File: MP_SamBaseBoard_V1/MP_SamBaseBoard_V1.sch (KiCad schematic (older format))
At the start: 129 parts, among them J1 MA_CONN, J10 P1_CONN, J11 I2C_CONN, J12 I2C_CONN, J13 SAM_SWD, J14 WS2812_EXT, J15 PWR_JACK, J16 USB_B_Micro, J17 BATT_CONN, J2 MB_CONN, J3 Adafruit_Feather_CONN, J4 LOAD_CONN, J5 SPEAKER, J7 SERVO_CONN, J8 P3_CONN, J9 P2_CONN, Q1 DMP3098L, Q2 ALS-PT19-315C/L177/TR8, SW1 RESET, SW2 3v3_PWR_SW, SW3 SW1, SW4 SW2, U1 ESP32-WROOM-32, U10 KXTJ3-1057, U13 SST25VF016B-50-4C-S2AF, U2 ATSAMD51J19A-A, U3 74LVC1G125, U4 TPS62135, U5 PAM8301, U6 BQ24075, U7 DRV8833RTY, U8 Sensirion_SHT3x, U9 LD39200PU33R, Y1 Crystal

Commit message: update
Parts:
- added Q3: BSS138-7-F, Package_TO_SOT_SMD:SOT-23, symbol Device:Q_NMOS_GSD
- added R12: 10K, Resistor_SMD:R_0603_1608Metric, symbol Device:R_Small
- added U12: IRFHM9331PbF, GiraffeTech-IR:PQFN_3x3mm_IRFHM9331TRPbF, symbol InGarage_FETs:IRFHM9331PbF
- gave numbers to parts that had none: 5
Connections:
- net +5V: now also U12.5 (DRAIN), U12.6 (DRAIN), U12.7 (DRAIN), U12.8 (DRAIN); no longer R8.1
- net GND: now also Q3.2 (S)
- net PG_5V: now also Q3.1 (G)
- net VIN: now also R8.1, R12.2, U12.1 (SOURCE), U12.2 (SOURCE), U12.3 (SOURCE)
- new net: Q3.3 (D), R12.1, U12.4 (GATE)
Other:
- moved on the sheet: BZ1, C10, C12, C13, C15, C16, C18, C29, C30, C31, C34, C35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

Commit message: finalize 1
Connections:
- net +3V3: no longer U10.3 (IO_VDD), U10.7 (VDD)
- no-connect marks 42 -> 44
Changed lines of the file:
@@
 Wire Wire Line
 	3750 9850 4500 9850
-Wire Wire Line
-	3750 9750 3750 9850
-Wire Wire Line
-	3750 9750 4500 9750
 Connection ~ 3750 9850
 NoConn ~ 5500 10200
@@
 $EndComp
 Wire Wire Line
-	3750 9650 3750 9750
-Connection ~ 3750 9750
-Wire Wire Line
-	4200 10000 4500 10000
-Wire Wire Line
-	4200 10100 4200 10000
-Wire Wire Line
 	3750 9850 3750 10200
 $Comp
@@
 	1    0    0    -1
 $EndComp
-Wire Wire Line
-	4200 9650 4200 10000
-Connection ~ 4200 10000
 Text Notes 9000 9350 0    50   ~ 0
 LIGHT SENSOR
@@
 	12150 1800 12150 1850
 Connection ~ 12150 1800
+Wire Wire Line
+	3750 9650 3750 9850
+Wire Wire Line
+	4200 9650 4200 10100
+Wire Wire Line
+	4400 9750 4500 9750
+Wire Wire Line
+	4400 10000 4500 10000
+NoConn ~ 4400 9750
+NoConn ~ 4400 10000
 $EndSCHEMATC

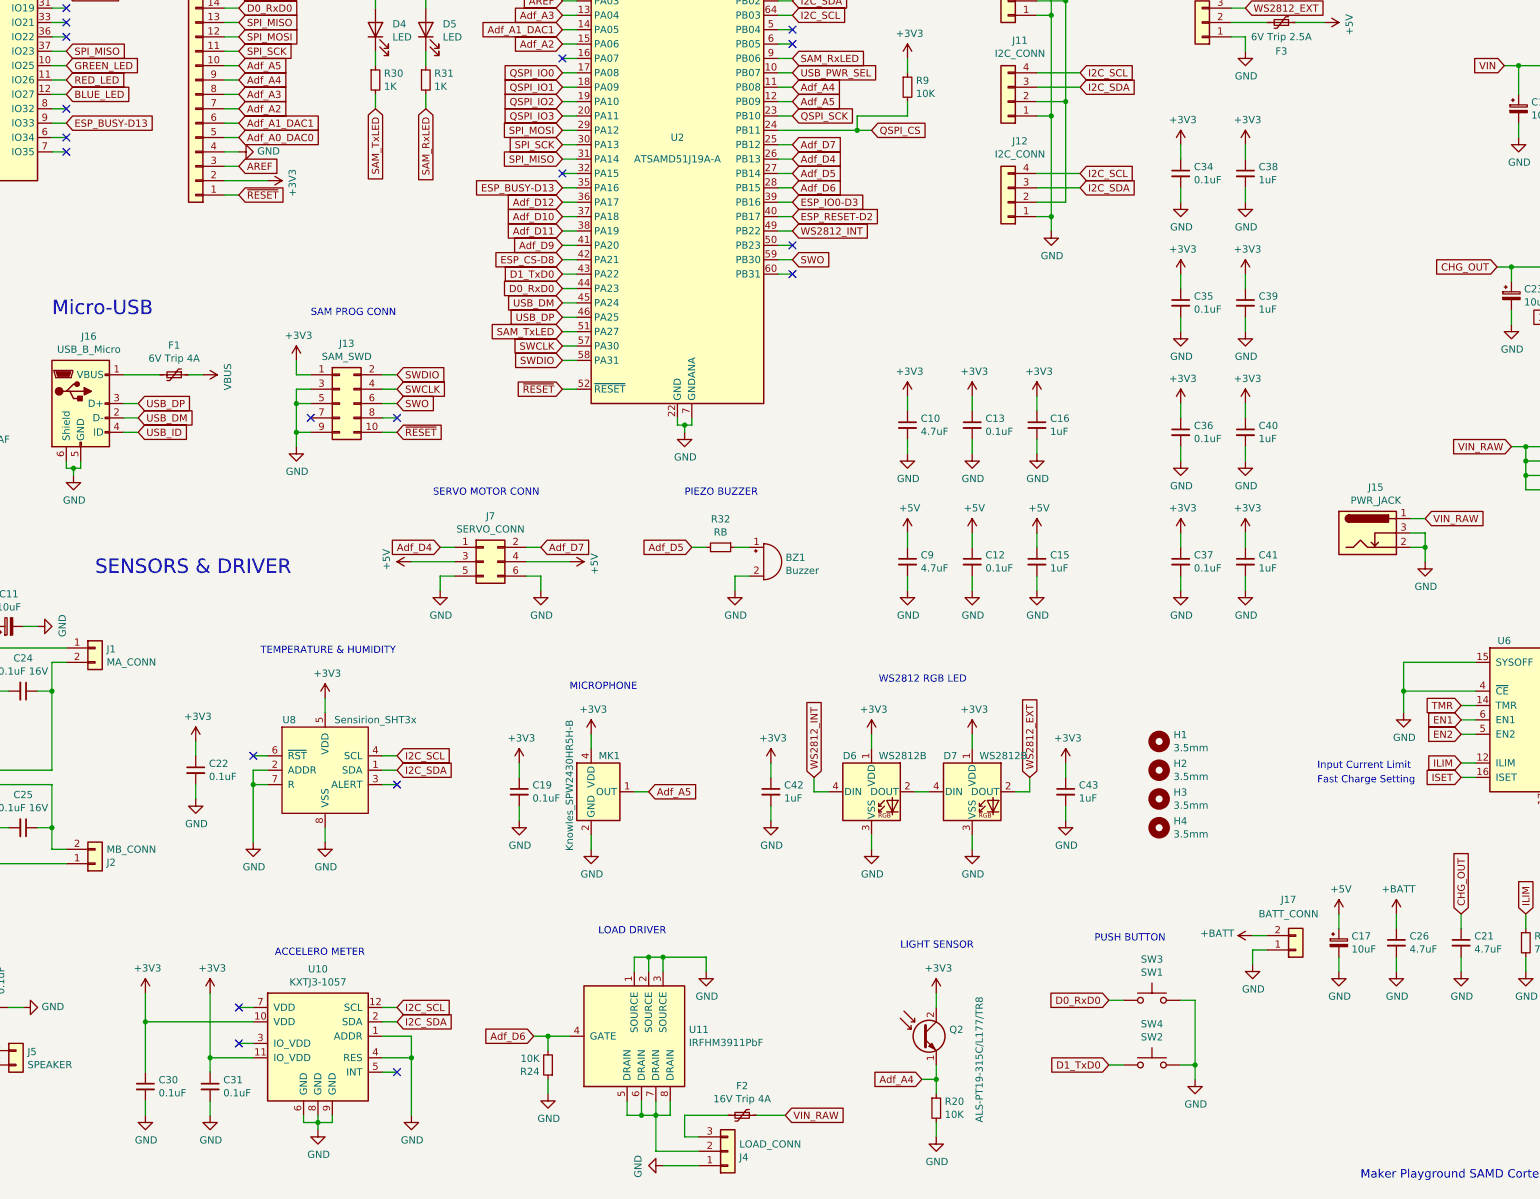
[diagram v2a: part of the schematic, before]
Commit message: Adding OLED display in progress
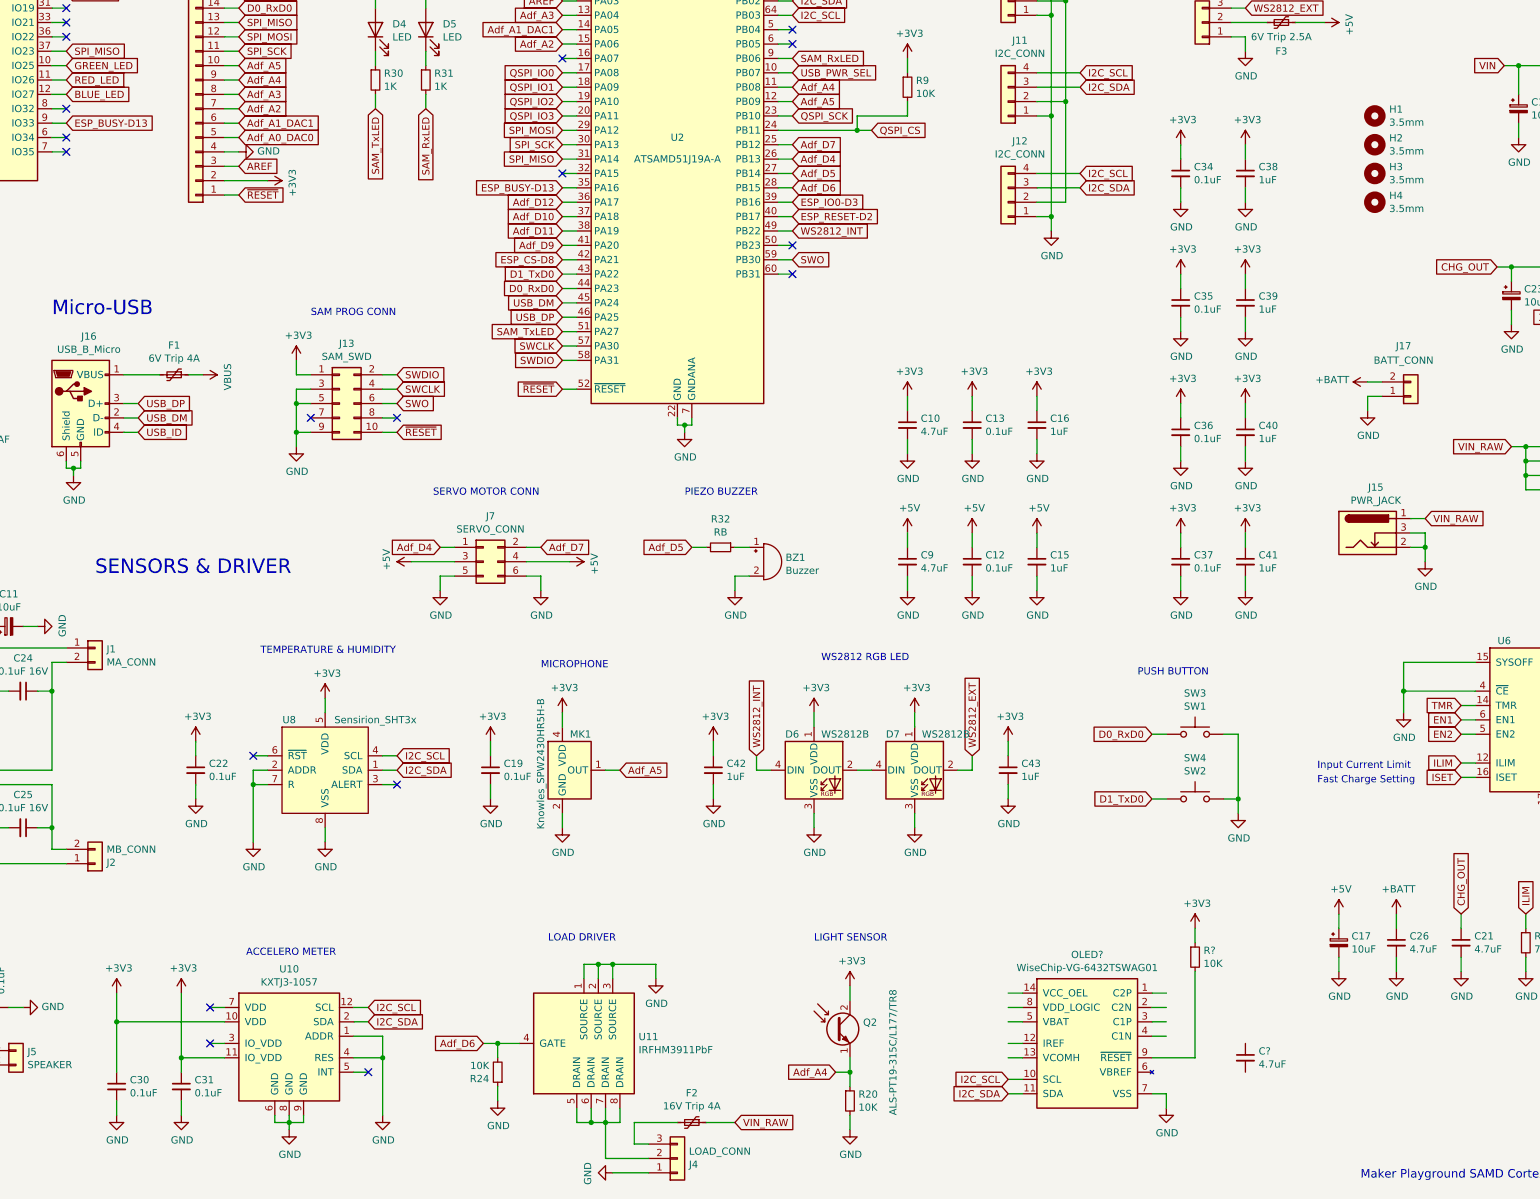
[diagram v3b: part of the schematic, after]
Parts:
- added C?: 4.7uF, Capacitor_SMD:C_0603_1608Metric, symbol Device:C_Small
- added OLED?: WiseChip-VG-6432TSWAG01, GiraffeTech-Connector:WiseChip-VG-6432TSWAG01, symbol InGarage_Display:WiseChip-VG-6432TSWAG01
- added R?: 10K, Resistor_SMD:R_0603_1608Metric, symbol Device:R_Small
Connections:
- net +3V3: now also R?.1
- net GND: now also OLED?.7 (VSS)
- net I2C_SCL: now also OLED?.10 (SCL)
- net I2C_SDA: now also OLED?.11 (SDA)
- new net: OLED?.9 (~RESET), R?.2
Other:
- moved on the sheet: C19, C30, C31, C42, C43, D6, D7, F2, H1, H2, H3, H4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

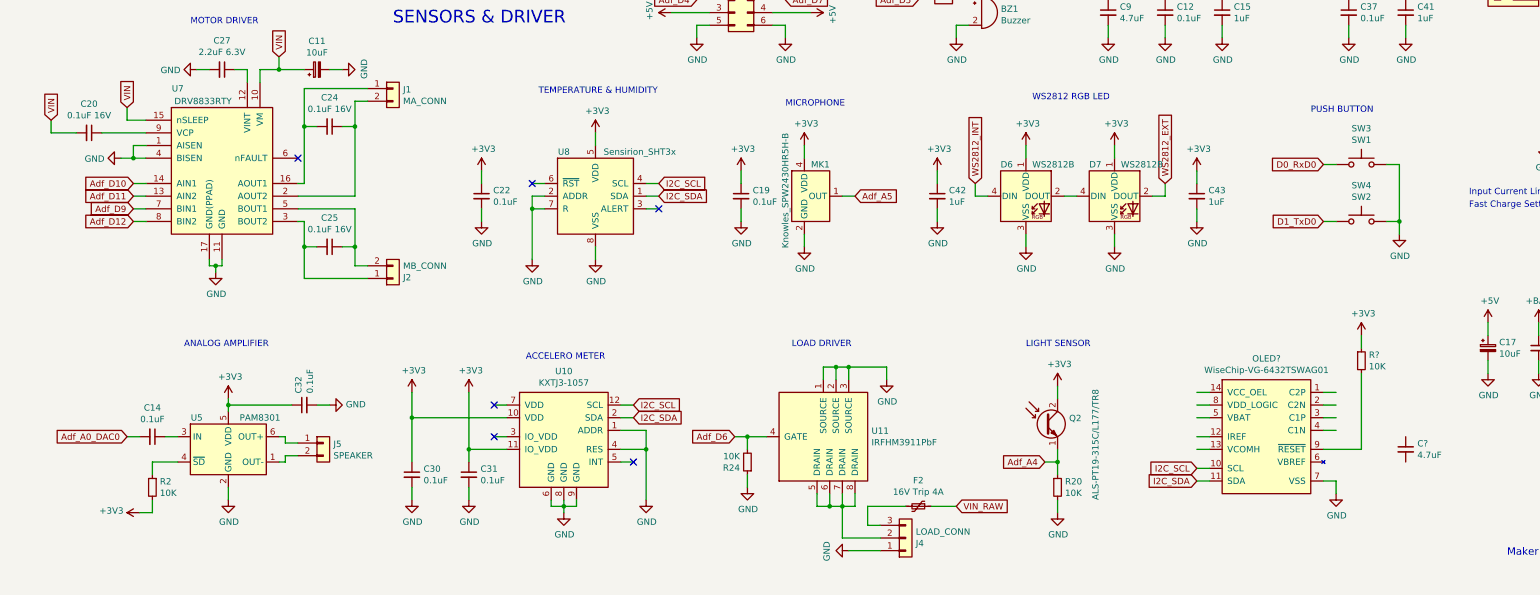
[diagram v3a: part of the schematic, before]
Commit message: Update OLED display, not complete
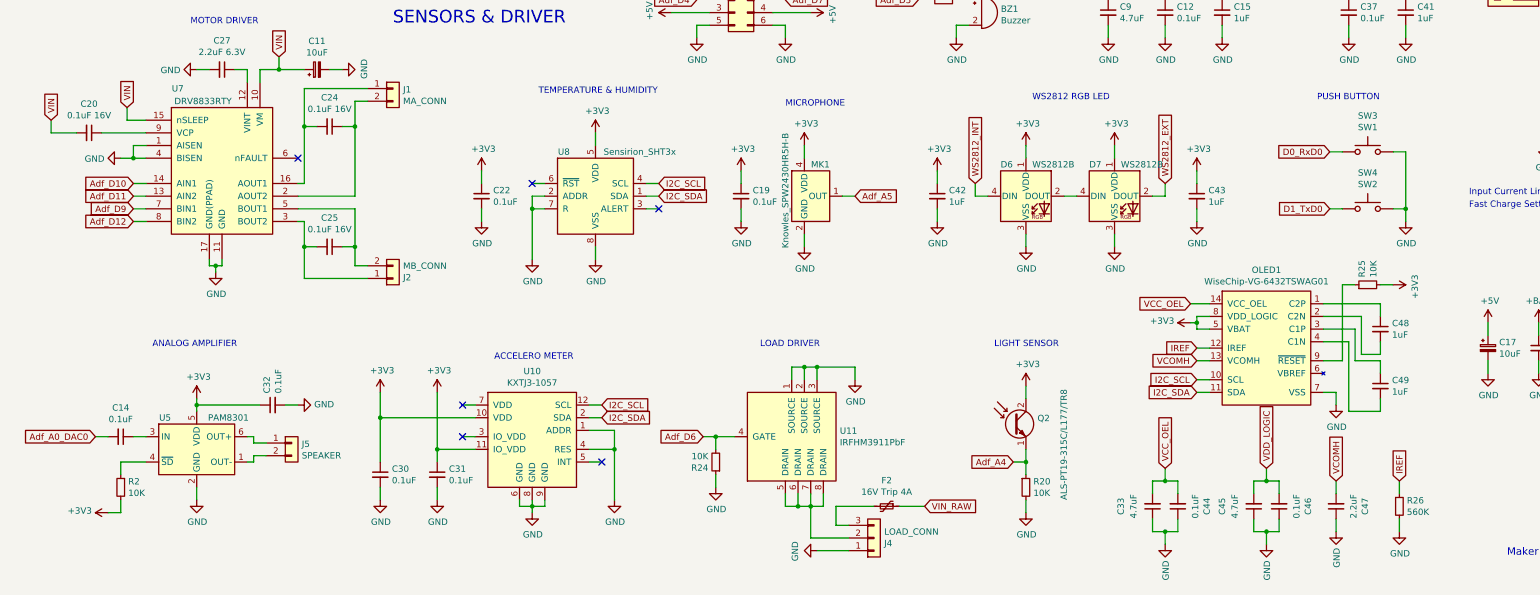
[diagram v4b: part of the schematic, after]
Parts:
- added C33, C45: 4.7uF, Capacitor_SMD:C_0603_1608Metric, symbol Device:C_Small
- added C44, C46: 0.1uF, Capacitor_SMD:C_0603_1608Metric, symbol Device:C_Small
- added C47: 2.2uF, Capacitor_SMD:C_0603_1608Metric, symbol Device:C_Small
- added C49: 1uF, Capacitor_SMD:C_0603_1608Metric, symbol Device:C_Small
- added R26: 560K, Resistor_SMD:R_0603_1608Metric, symbol Device:R_Small
- C48: renamed from C?; value 4.7uF -> 1uF
- gave numbers to parts that had none: 2
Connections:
- net +3V3: now also OLED1.5 (VBAT), OLED1.8 (VDD_LOGIC), R25.2; no longer R25.1
- net GND: now also C33.1, C44.1, C45.1, C46.1, C47.1, R26.2
- net at OLED1.1 (C2P): now also C48.1
- net IREF: now reaches OLED1.12 (IREF)
- net IREF: now also R26.1
- net VCOMH: now reaches OLED1.13 (VCOMH)
- net VCOMH: now also C47.2
- net VCC_OEL: now reaches OLED1.14 (VCC_OEL)
- net VCC_OEL: now also C33.2, C44.2
- net at OLED1.2 (C2N): now also C48.2
- net at OLED1.3 (C1P): now also C49.1
- net at OLED1.4 (C1N): now also C49.2
- net at OLED1.9 (~RESET): now also R25.1; no longer R25.2
- new net VDD_LOGIC: C45.2, C46.2
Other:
- moved on the sheet: C14, C30, C31, C32, C48, F2, J4, J5, OLED1, Q2, R2, R20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
